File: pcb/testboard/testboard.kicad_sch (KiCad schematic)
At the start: 0 parts

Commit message: Manual branch merge Merged branches for USB POWER and MOTOR DRIVER modules; Finished the first version of the schematic
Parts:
- added J1: Left Socket, Connector_PinSocket_2.54mm:PinSocket_1x20_P2.54mm_Vertical, symbol Connector:Conn_01x20_Socket
- added J2: Right Socket, Connector_PinSocket_2.54mm:PinSocket_1x20_P2.54mm_Vertical, symbol Connector:Conn_01x20_Socket
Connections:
- new net 3V3: J1.20 (Pin_20), J2.3 (Pin_3)
- new net 5V: J1.18 (Pin_18)
- new net GND: J1.19 (Pin_19), J2.1 (Pin_1), J2.2 (Pin_2)
- new net NRST: J2.4 (Pin_4)
- new net PA0: J2.16 (Pin_16)
- new net PA1: J2.15 (Pin_15)
- new net PA10: J1.7 (Pin_7)
- new net PA11: J1.8 (Pin_8)
- new net PA12: J1.9 (Pin_9)
- new net PA15: J1.10 (Pin_10)
- new net PA2: J2.14 (Pin_14)
- new net PA3: J2.13 (Pin_13)
- new net PA4: J2.12 (Pin_12)
- new net PA5: J2.11 (Pin_11)
- new net PA6: J2.10 (Pin_10)
- new net PA7: J2.9 (Pin_9)
- new net PA8: J1.5 (Pin_5)
- new net PA9: J1.6 (Pin_6)
- new net PB0: J2.8 (Pin_8)
- new net PB1: J2.7 (Pin_7)
- new net PB10: J2.6 (Pin_6)
- new net PB11: J2.5 (Pin_5)
- new net PB12: J1.1 (Pin_1)
- new net PB13: J1.2 (Pin_2)
- new net PB14: J1.3 (Pin_3)
- new net PB15: J1.4 (Pin_4)
- new net PB3: J1.11 (Pin_11)
- new net PB4: J1.12 (Pin_12)
- new net PB5: J1.13 (Pin_13)
- new net PB6: J1.14 (Pin_14)
- new net PB7: J1.15 (Pin_15)
- new net PB8: J1.16 (Pin_16)
- new net PB9: J1.17 (Pin_17)
- new net PC13: J2.19 (Pin_19)
- new net PC14: J2.18 (Pin_18)
- new net PC15: J2.17 (Pin_17)
- new net VBAT: J2.20 (Pin_20)
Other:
- added sheet MOTOR DRIVER (motor_drive.kicad_sch)
- added sheet USB POWER (usb_power.kicad_sch)
- note added: "STM32 Bluepill"

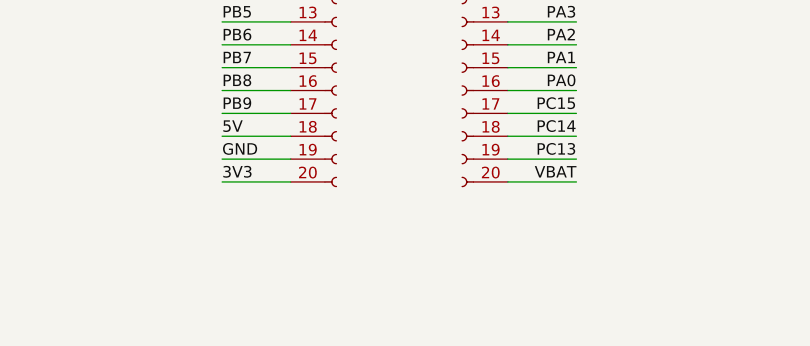
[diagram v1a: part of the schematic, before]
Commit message: Schematic final edit Added all remaining components and modifications, started PCB design
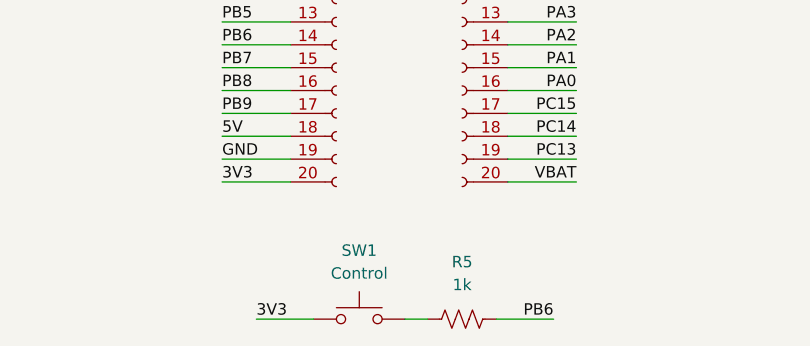
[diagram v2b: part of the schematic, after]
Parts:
- added R5: 1k, Resistor_SMD:R_0805_2012Metric, symbol Device:R_US
- added SW1: Control, Button_Switch_THT:SW_PUSH-12mm, symbol Switch:SW_Push
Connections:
- net 3V3: now also SW1.1
- net PB6: now also R5.2
- new net: R5.1, SW1.2
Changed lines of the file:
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@@
+	(wire
+		(pts
+			(xy 114.3 116.84) (xy 120.65 116.84)
+		)
+		(stroke
+			(width 0)
+			(type default)
+		)
+	)
 	(wire
 		(pts
@@
 	(wire
 		(pts
+			(xy 130.81 116.84) (xy 133.35 116.84)
+		)
+		(stroke
+			(width 0)
+			(type default)
+		)
+	)
+	(wire
+		(pts
 			(xy 110.49 63.5) (xy 118.11 63.5)
 		)
@@
 		(pts
 			(xy 142.24 93.98) (xy 149.86 93.98)
+		)
+		(stroke
+			(width 0)
+			(type default)
+		)
+	)
+	(wire
+		(pts
+			(xy 140.97 116.84) (xy 147.32 116.84)
 		)
 		(stroke
@@
 		)
 	)
+	(label "3V3"
+		(at 114.3 116.84 0)
+		(effects
+			(font
+				(size 1.27 1.27)
+			)
+			(justify left bottom)
+		)
+	)
 	(label "PB0"
 		(at 149.86 71.12 180)
@@
 			)
 			(justify left bottom)
+		)
+	)
+	(label "PB6"
+		(at 147.32 116.84 180)
+		(effects
+			(font
+				(size 1.27 1.27)
+			)
+			(justify right bottom)
 		)
 	)
@@
 					(unit 1)
 				)
+			)
+		)
+	)
+	(symbol
+		(lib_id "Device:R_US")
+		(at 137.16 116.84 90)
+		(unit 1)
+		(body_style 1)
+		(exclude_from_sim no)
+		(in_bom yes)
+		(on_board yes)
+		(in_pos_files yes)
+		(dnp no)
+		(fields_autoplaced yes)
+		(property "Reference" "R5"
+			(at 137.16 110.49 90)
+			(show_name no)
+			(do_not_autoplace no)
+			(effects
+				(font
+					(size 1.27 1.27)
+				)
+			)
+		)
+		(property "Value" "1k"
+			(at 137.16 113.03 90)
+			(show_name no)
+			(do_not_autoplace no)
+			(effects
+				(font
+					(size 1.27 1.27)
+				)
+			)
+		)
+		(property "Footprint" "Resistor_SMD:R_0805_2012Metric"
+			(at 137.414 115.824 90)
+			(hide yes)
+			(show_name no)
+			(do_not_autoplace no)
+			(effects
+				(font
+					(size 1.27 1.27)
+				)
+			)
+		)
+		(property "Datasheet" ""
+			(at 137.16 116.84 0)
+			(hide yes)
+			(show_name no)
+			(do_not_autoplace no)
+			(effects
+				(font
+					(size 1.27 1.27)
+				)
+			)
+		)
+		(property "Description" "Resistor, US symbol"
+			(at 137.16 116.84 0)
+			(hide yes)
+			(show_name no)
+			(do_not_autoplace no)
+			(effects
+				(font
+					(size 1.27 1.27)
+				)
+			)
+		)
+		(pin "2"
+		)
+		(pin "1"
+		)
+		(instances
+			(project "testboard"
+				(path "/043d0279-5e5f-4026-8fb9-7ba8619eaf91"
+					(reference "R5")
+					(unit 1)
+				)
+			)
+		)
+	)
+	(symbol
+		(lib_id "Switch:SW_Push")
+		(at 125.73 116.84 0)
+		(unit 1)
+		(body_style 1)
+		(exclude_from_sim no)
+		(in_bom yes)
+		(on_board yes)
+		(in_pos_files yes)
+		(dnp no)
+		(fields_autoplaced yes)
+		(property "Reference" "SW1"
+			(at 125.73 109.22 0)
+			(show_name no)
+			(do_not_autoplace no)
+			(effects
+				(font
+					(size 1.27 1.27)
+				)
+			)
+		)
+		(property "Value" "Control"
+			(at 125.73 111.76 0)
+			(show_name no)
+			(do_not_autoplace no)
+			(effects
+				(font
+					(size 1.27 1.27)
+				)
+			)
+		)
+		(property "Footprint" "Button_Switch_THT:SW_PUSH-12mm"
+			(at 125.73 111.76 0)
+			(hide yes)
+			(show_name no)
+			(do_not_autoplace no)
+			(effects
+				(font
+					(size 1.27 1.27)
+				)
+			)
+		)
+		(property "Datasheet" ""
+			(at 125.73 111.76 0)
+			(hide yes)
+			(show_name no)
+			(do_not_autoplace no)
+			(effects
+				(font
+					(size 1.27 1.27)
+				)
+			)
+		)
+		(property "Description" "Push button switch, generic, two pins"
+			(at 125.73 116.84 0)
+			(hide yes)
+			(show_name no)
+			(do_not_autoplace no)
+			(effects
+				(font
+					(size 1.27 1.27)
+				)
+			)
+		)
+		(pin "1"
+		)
+		(pin "2"
+		)
+		(instances
+			(project "testboard"
+				(path "/043d0279-5e5f-4026-8fb9-7ba8619eaf91"
+					(reference "SW1")
+					(unit 1)
+				)
